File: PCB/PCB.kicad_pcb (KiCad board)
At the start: 2 copper layers, 94.5 x 55.5 mm, 19 parts, among them J1 Conn_01x04_Pin, J2 Conn_01x05_Pin, J3 Conn_01x04_Pin, SW1 SW_SPDT, SW2 SW_Push, U1 ESP32-DevKitC

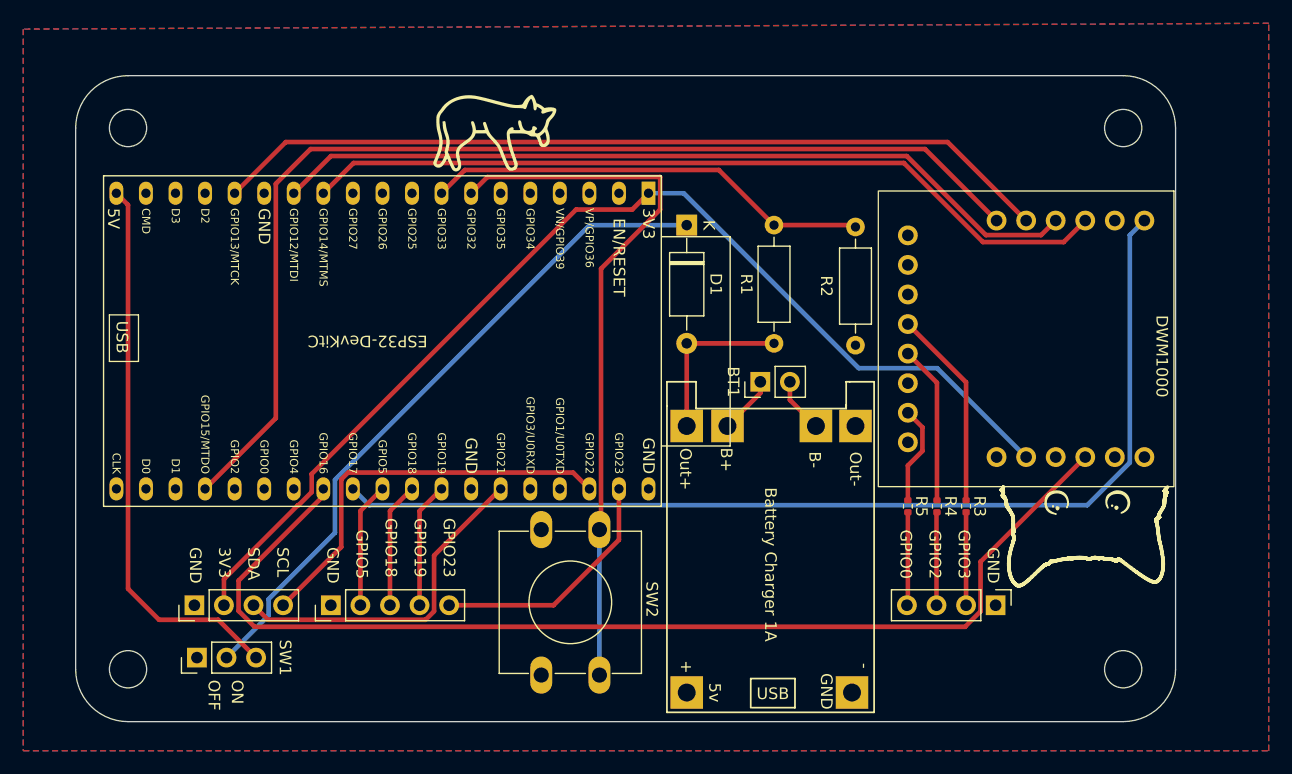
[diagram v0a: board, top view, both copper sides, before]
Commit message: repaired the size of an esp
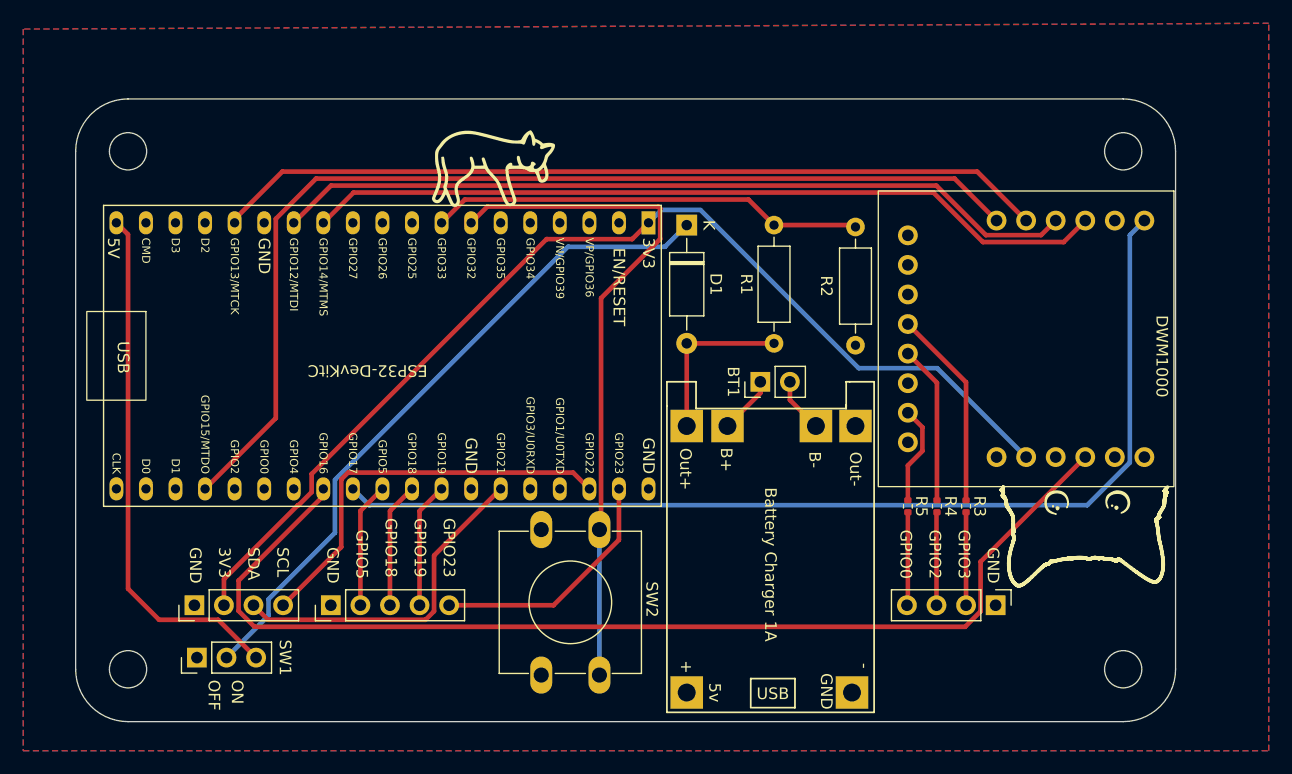
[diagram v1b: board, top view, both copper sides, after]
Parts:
- moved U1 2.54 mm to (104.1, 75.3)
- moved H1 2.00 mm to (59.4, 69.2)
- moved H2 2.00 mm to (144.9, 69.2)
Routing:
- net /CS: track 94.4 -> 90.6 mm
- net Net-(U1-32K_XP/GPIO32/ADC1_CH4): track 61.8 -> 59.1 mm
- net Net-(SW1-C): track 47.8 -> 45.3 mm
- net +3.3V: track 95.2 -> 94.0 mm
- net VBAT: track 38.4 -> 37.4 mm
- net /MISO: track 70.1 -> 69.1 mm
- net /CLK: track 70.1 -> 69.1 mm
- net /MOSI: track 72.6 -> 71.7 mm
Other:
- board size 94.5 x 55.5 mm -> 94.5 x 53.5 mm
- board text removed: "USB"

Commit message: added pins for motor encoders
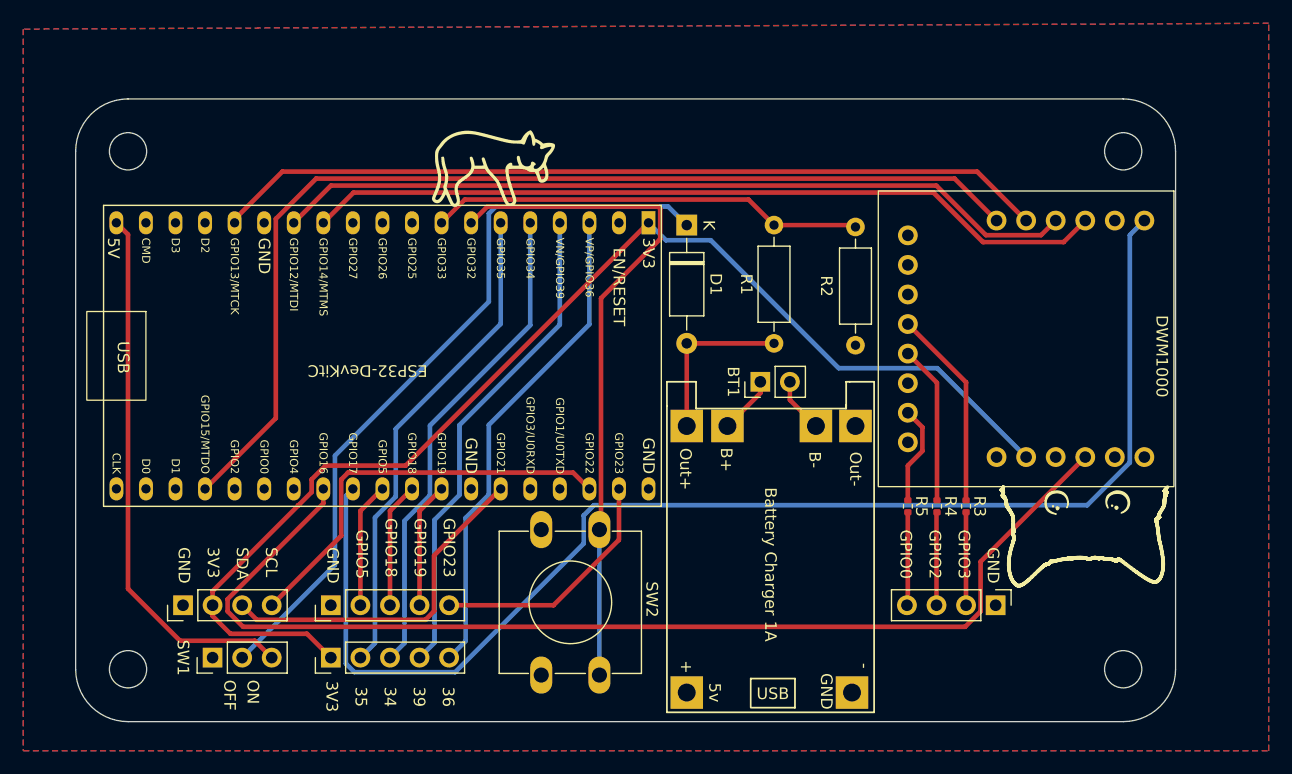
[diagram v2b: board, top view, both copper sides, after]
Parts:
- added J4: Conn_01x05_Pin, Connector_PinHeader_2.54mm:PinHeader_1x05_P2.54mm_Vertical, F.Cu at (76.8, 112.7)
- moved SW1 1.35 mm to (66.7, 112.7)
- moved J1 0.97 mm to (64.1, 108.2)
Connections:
- U1 pad 3: unconnected-(U1-SENSOR_VP/GPIO36/ADC1_CH0-Pad3) -> /GPIO36
- U1 pad 4: unconnected-(U1-SENSOR_VN/GPIO39/ADC1_CH3-Pad4) -> /GPIO39
- U1 pad 5: unconnected-(U1-VDET_1/GPIO34/ADC1_CH6-Pad5) -> /GPIO34
- U1 pad 6: unconnected-(U1-VDET_2/GPIO35/ADC1_CH7-Pad6) -> /GPIO35
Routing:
- net /GPIO39: track 0.00 -> 42.3 mm
- net /GPIO35: track 0.00 -> 42.3 mm
- net /GPIO34: track 0.00 -> 42.3 mm
- net /GPIO36: track 0.00 -> 42.3 mm
- net /IRQ: track 90.2 -> 113.1 mm
- net +3.3V: track 94.0 -> 105.8 mm
- net +5V: track 58.4 -> 64.8 mm
- net /RST: track 95.3 -> 96.7 mm
- net Net-(SW1-C): track 45.3 -> 46.6 mm
- net /SDA: track 29.2 -> 30.2 mm
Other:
- board text added: "34"
- board text added: "35"
- board text added: "36"
- board text added: "39"

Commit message: new header for encoders, adjusted resitor values
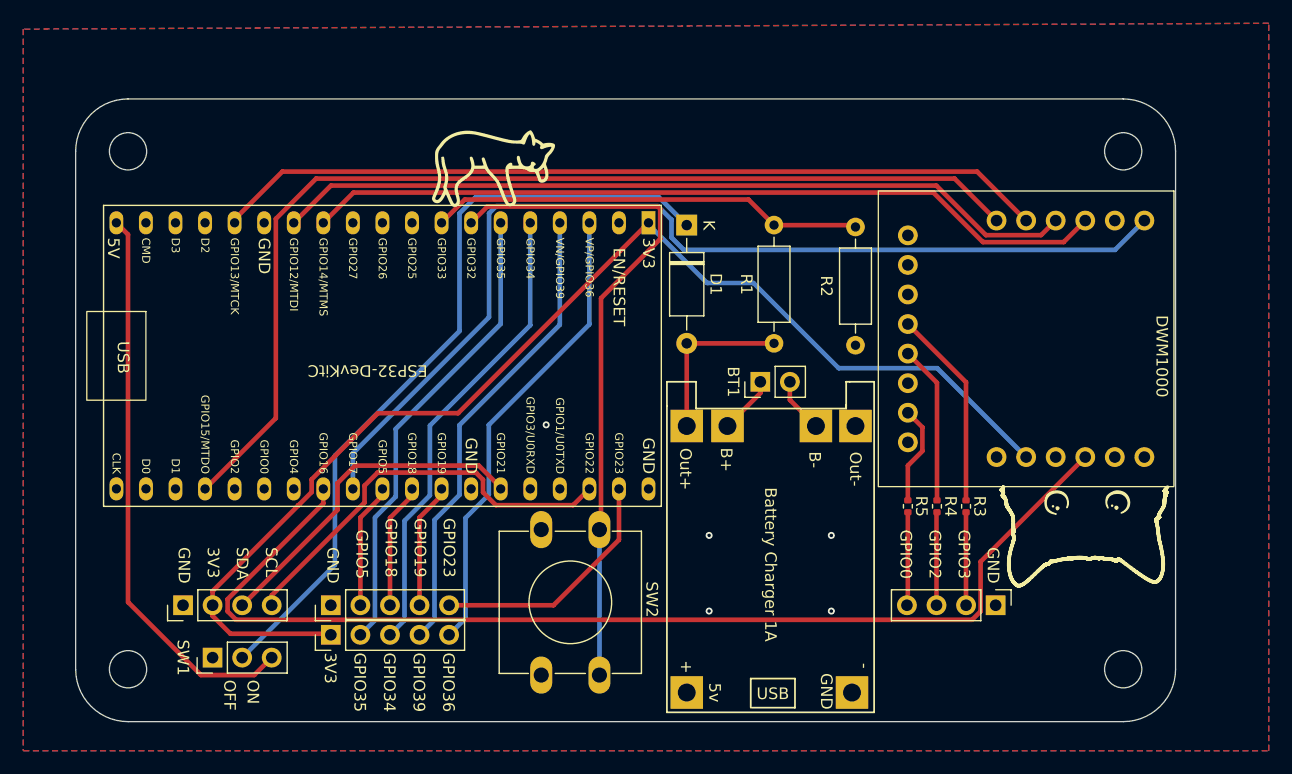
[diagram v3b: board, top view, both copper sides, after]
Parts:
- moved J4 1.96 mm to (76.8, 110.7)
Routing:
- net /IRQ: track 113.1 -> 88.6 mm
- net +5V: track 64.8 -> 67.0 mm
- net /GPIO34: track 42.3 -> 40.4 mm
- net /GPIO39: track 42.3 -> 40.4 mm
- net /GPIO36: track 42.3 -> 40.4 mm
- net /GPIO35: track 42.3 -> 40.4 mm
- net Net-(SW1-C): track 46.6 -> 48.6 mm
- net /SDA: track 30.2 -> 29.4 mm
- net +3.3V: track 105.8 -> 105.1 mm
- net GND: vias 0 -> 5
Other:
- board text added: "GPIO34"
- board text added: "GPIO35"
- board text added: "GPIO36"
- board text added: "GPIO39"
- board text removed: "34"
- board text removed: "35"
- board text removed: "36"
- board text removed: "39"

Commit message: fix: fixed wrong wiring of the UWB
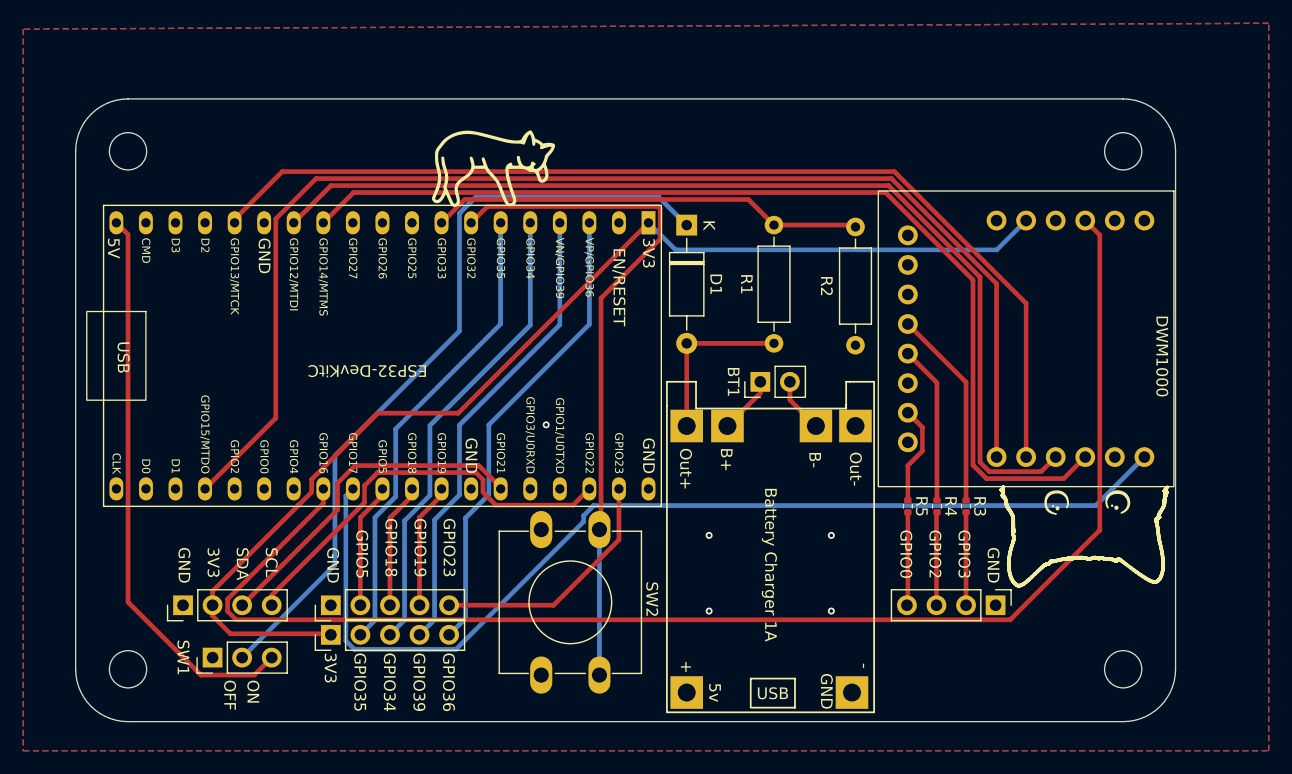
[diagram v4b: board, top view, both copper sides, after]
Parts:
- R3, R4, R5: value 10k -> 150
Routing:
- net /RST: track 96.2 -> 119.5 mm
- net /MISO: track 69.1 -> 86.8 mm
- net /CLK: track 69.1 -> 86.8 mm
- net /CS: track 90.6 -> 107.7 mm
- net /MOSI: track 71.7 -> 87.9 mm
- net +3.3V: track 105.1 -> 98.8 mm
- net /IRQ: track 88.6 -> 89.4 mm
